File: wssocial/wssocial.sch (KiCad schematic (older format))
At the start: 47 parts, among them J11 18Vac, J3 Batería, J7 SIL-100-05, J8 SIL-100-05, Q2 BC817, Q3 MMBF2202PT1, U2 LM2596S-5, U4 PC817D

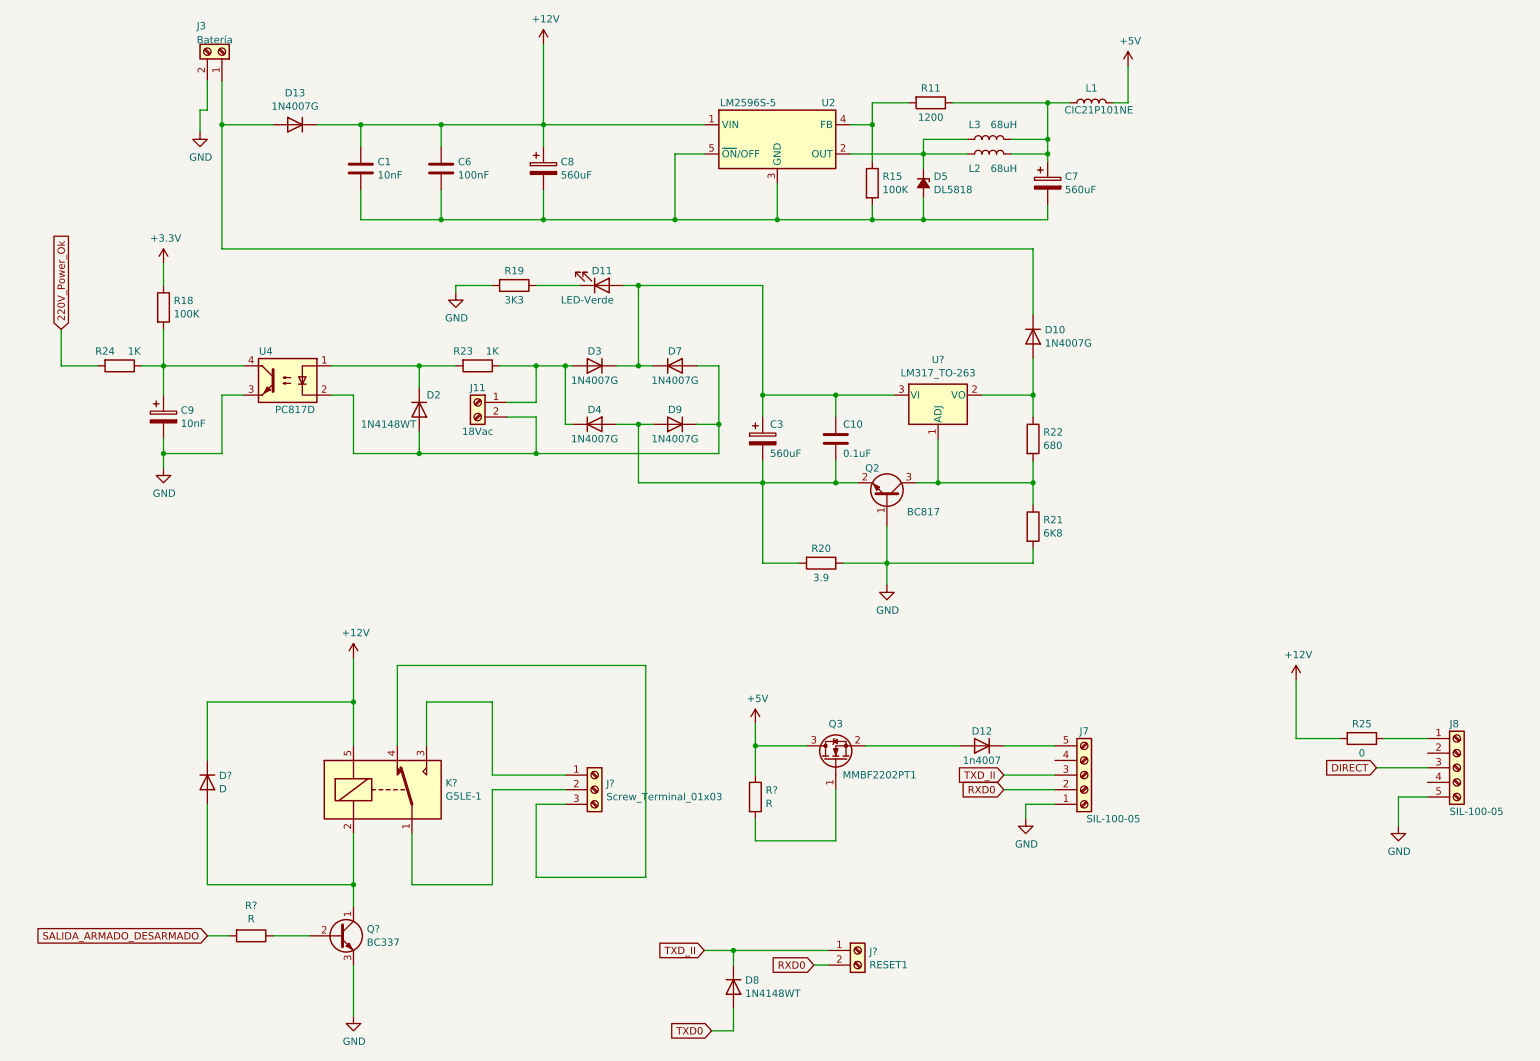
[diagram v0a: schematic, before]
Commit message: make hierarchical sheets in layout
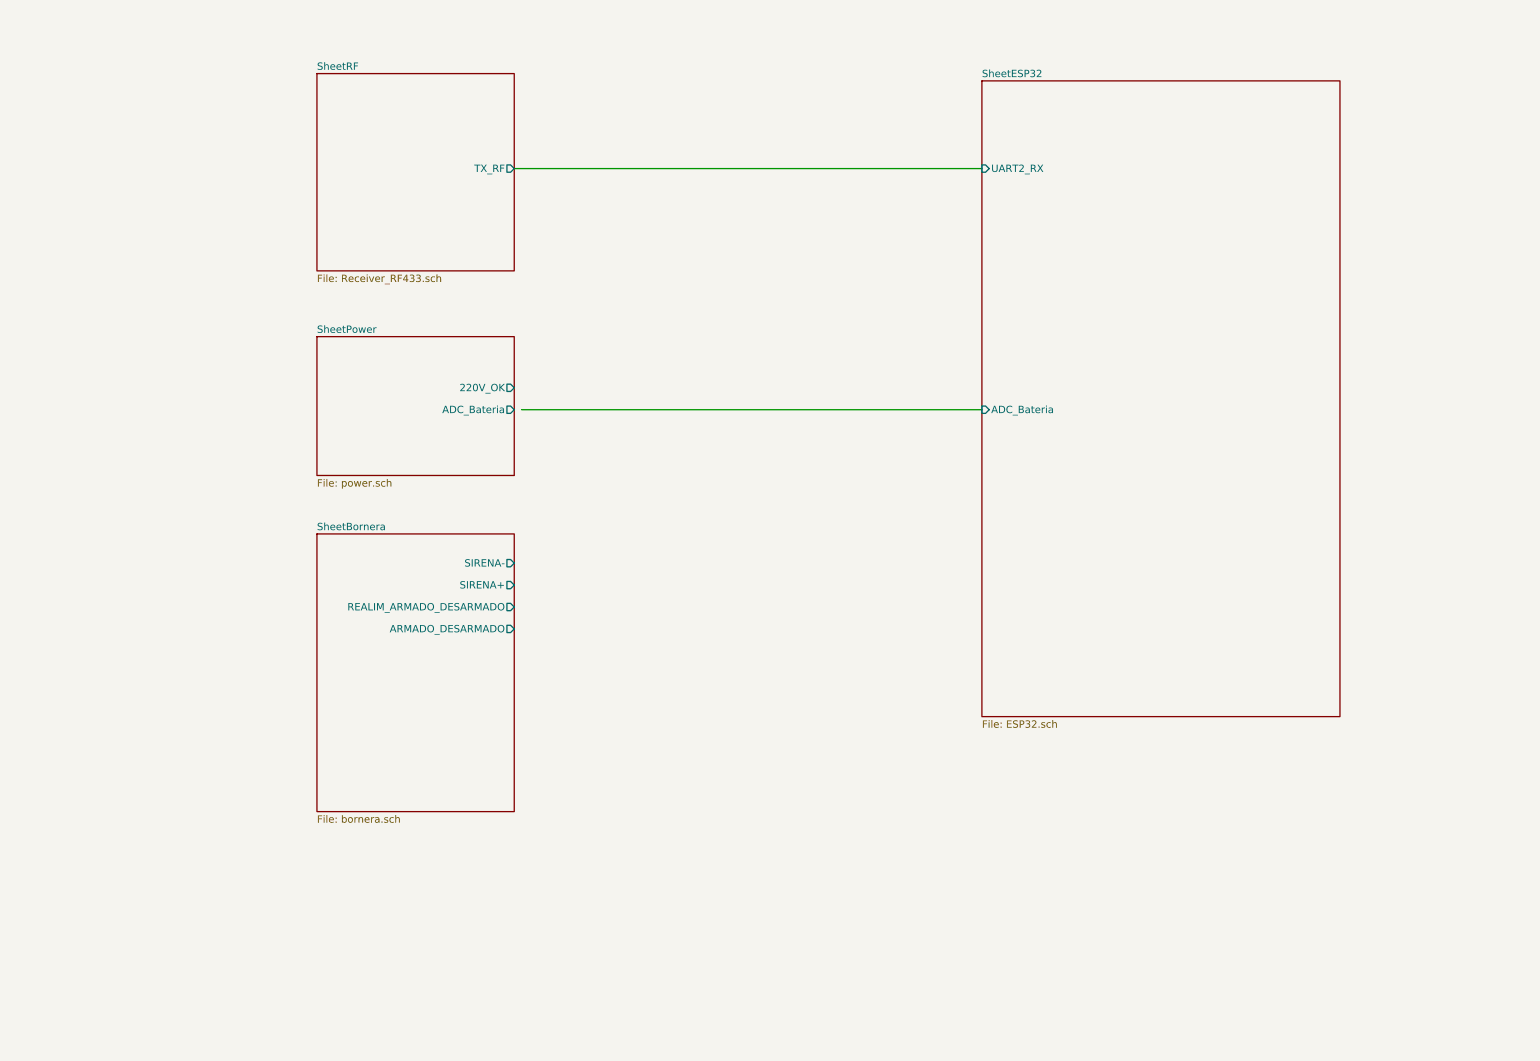
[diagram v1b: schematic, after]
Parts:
- removed C1: 10nF, symbol Device:C
- removed C10: 0.1uF, symbol Device:C
- removed C3, C7, C8: 560uF, symbol Device:CP
- removed C6: 100nF, symbol Device:C
- removed C9: 10nF, symbol Device:CP
- removed D10: 1N4007G, symbol Device:D
- removed D11: LED-Verde, symbol Device:LED
- removed D12: 1n4007, symbol Device:D
- removed D13, D3, D4, D7, D9: 1N4007G, Diode_THT:D_DO-41_SOD81_P10.16mm_Horizontal, symbol Diode:1N4007
- removed D2, D8: 1N4148WT, symbol Device:D
- removed D5: DL5818, symbol Device:D_Zener_Small_ALT
- removed D?: D, symbol Device:D
- removed J11: 18Vac, symbol Connector:Screw_Terminal_01x02
- removed J3: Batería, symbol Connector:Screw_Terminal_01x02
- removed J7, J8: SIL-100-05, symbol Connector:Screw_Terminal_01x05
- removed J?: Screw_Terminal_01x03, symbol Connector:Screw_Terminal_01x03
- removed J?: RESET1, symbol Connector:Screw_Terminal_01x02
- removed K?: G5LE-1, Relay_THT:Relay_SPDT_Omron-G5LE-1, symbol Relay:G5LE-1
- removed L1: CIC21P101NE, symbol Device:L
- removed L2, L3: 68uH, symbol Device:L
- removed Q2: BC817, Package_TO_SOT_SMD:SOT-23, symbol Transistor_BJT:BC817
- removed Q3: MMBF2202PT1, Package_TO_SOT_SMD:SOT-23, symbol Transistor_FET:MMBF170
- removed Q?: BC337, Package_TO_SOT_THT:TO-92_Inline, symbol Transistor_BJT:BC337
- removed R11: 1200, symbol Device:R
- removed R15, R18: 100K, symbol Device:R
- removed R19: 3K3, symbol Device:R
- removed R20: 3.9, symbol Device:R
- removed R21: 6K8, symbol Device:R
- removed R22: 680, symbol Device:R
- removed R23, R24: 1K, symbol Device:R
- removed R25: 0, symbol Device:R
- removed R? (x2): R, symbol Device:R
- removed U2: LM2596S-5, Package_TO_SOT_SMD:TO-263-5_TabPin3, symbol Regulator_Switching:LM2596S-5
- removed U4: PC817D, Package_DIP:DIP-4_W7.62mm, symbol Isolator:PC817
- removed U?: LM317_TO-263, Package_TO_SOT_SMD:TO-263-2, symbol Regulator_Linear:LM317_TO-263
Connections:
- net labels removed: +12V, +3.3V, +5V, 220V_Power_Ok, DIRECT, GND, RXD0, SALIDA_ARMADO_DESARMADO, TXD0, TXD_II
- wire segments 169 -> 2
